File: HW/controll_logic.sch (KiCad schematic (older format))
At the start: 11 parts, among them SW1 RESET, U10 TL7705B, U9 74HC74, X2 8MHz

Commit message: Address, databus and control signals added to RAM and ROM
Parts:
- added U?: ispMACH4A, symbol ispMACH4A
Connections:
- net labels added: ~DUARTSEL, ~RTCSEL, ~VIA1SEL, ~VIA2SEL
- wire segments 60 -> 74
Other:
- moved on the sheet: SW1
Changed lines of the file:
@@
 encoding utf-8
 Sheet 5 6
-Title ""
-Date ""
-Rev ""
-Comp ""
+Title "Glue and control logic"
+Date "2017-12-23"
+Rev "0.1"
+Comp "Linux Grotto"
 Comment1 ""
 Comment2 ""
@@
 L R_Network07 RN2
 U 1 1 5A3B46CC
-P 6600 1550
-F 0 "RN2" V 6200 1550 50  0000 C CNN
-F 1 "3.3kOhm" V 7000 1550 50  0000 C CNN
-F 2 "Resistors_THT:R_Array_SIP8" V 7075 1550 50  0001 C CNN
-F 3 "" H 6600 1550 50  0001 C CNN
-	1    6600 1550
+P 1750 1100
+F 0 "RN2" V 1350 1100 50  0000 C CNN
+F 1 "3.3kOhm" V 2150 1100 50  0000 C CNN
+F 2 "Resistors_THT:R_Array_SIP8" V 2225 1100 50  0001 C CNN
+F 3 "" H 1750 1100 50  0001 C CNN
+	1    1750 1100
 	1    0    0    -1
 $EndComp
@@
 CLK
 NoConn ~ 2350 6625
-Wire Wire Line
-	2950 6625 3225 6625
-Wire Wire Line
-	2650 6075 2650 6325
-Wire Wire Line
-	2650 6075 3825 6075
-Wire Wire Line
-	3825 7175 3075 7175
-Wire Wire Line
-	3075 7175 3075 6075
-Connection ~ 3075 6075
-Wire Wire Line
-	4425 6825 4575 6825
-Wire Wire Line
-	4575 6825 4575 5975
-Wire Wire Line
-	4575 5975 3225 5975
-Wire Wire Line
-	3225 5975 3225 6425
-Wire Wire Line
-	4425 6425 4850 6425
-Wire Wire Line
-	2650 6925 2650 7050
-Wire Wire Line
-	1300 6075 700  6075
-Wire Wire Line
-	700  6075 700  7375
-Connection ~ 700  6425
-Connection ~ 700  6625
-Wire Wire Line
-	1300 7175 700  7175
-Connection ~ 700  7175
 NoConn ~ 1900 6425
 NoConn ~ 1900 6825
@@
 	1    0    0    -1
 $EndComp
-Wire Wire Line
-	3925 1350 3925 1150
-Wire Wire Line
-	4525 1750 4525 1925
-Wire Wire Line
-	4525 1925 4750 1925
-Wire Wire Line
-	4425 1750 4425 2025
-Wire Wire Line
-	4425 2025 4750 2025
-Wire Wire Line
-	4325 1750 4325 2125
-Wire Wire Line
-	4325 2125 4750 2125
-Wire Wire Line
-	4225 1750 4225 2225
-Wire Wire Line
-	4225 2225 4750 2225
-Wire Wire Line
-	4125 1750 4125 2325
-Wire Wire Line
-	4125 2325 4750 2325
-Wire Wire Line
-	4025 1750 4025 2425
-Wire Wire Line
-	4025 2425 4750 2425
-Wire Wire Line
-	3925 1750 3925 2825
-Wire Wire Line
-	3925 2525 4750 2525
 Text HLabel 4750 1925 2    60   BiDi ~ 0
 ~IRQ
@@
 Text HLabel 4750 2325 2    60   Output ~ 0
 ~SO
-Connection ~ 3925 2525
 Text HLabel 4750 2625 2    60   Output ~ 0
 RES
-Wire Wire Line
-	3925 3050 4250 3050
-Wire Wire Line
-	4250 2625 4250 3375
-Wire Wire Line
-	4250 2625 4750 2625
 $Comp
 L C_Small C15
@@
 F 3 "" H 2000 3575 50  0001 C CNN
 	1    2000 3375
-	0    1    1    0
-$EndComp
-Wire Wire Line
-	2325 3275 2325 3375
-Wire Wire Line
-	2325 3575 2325 3650
+	0    -1   -1   0
+$EndComp
 $Comp
 L GND #PWR16
@@
 	1    0    0    -1
 $EndComp
-Wire Wire Line
-	2000 3850 4250 3850
-Wire Wire Line
-	3125 3850 3125 3600
 $Comp
 L VCC #PWR13
@@
 	1    0    0    -1
 $EndComp
-Wire Wire Line
-	2000 2500 3125 2500
+$Comp
+L VCC #PWR18
+U 1 1 5A3BAB89
+P 1450 700
+F 0 "#PWR18" H 1450 550 50  0001 C CNN
+F 1 "VCC" H 1450 850 50  0000 C CNN
+F 2 "" H 1450 700 50  0001 C CNN
+F 3 "" H 1450 700 50  0001 C CNN
+	1    1450 700
+	1    0    0    -1
+$EndComp
+Text HLabel 2300 1475 2    60   Input ~ 0
+TCK
+Text HLabel 2300 1575 2    60   Input ~ 0
+TMS
+Text HLabel 2300 1675 2    60   Input ~ 0
+TDI
+Text HLabel 2300 1775 2    60   Output ~ 0
+TDO
+Text HLabel 2300 1875 2    60   Output ~ 0
+~KS
+$Comp
+L ispMACH4A U?
+U 1 1 5A3F3D11
+P 8275 2325
+F 0 "U?" H 8275 3775 60  0000 C CNN
+F 1 "ispMACH4A" V 8275 1950 60  0000 C CNN
+F 2 "" H 7950 2300 60  0001 C CNN
+F 3 "" H 7950 2300 60  0001 C CNN
+	1    8275 2325
+	1    0    0    -1
+$EndComp
+Text HLabel 7250 3075 0    60   Output ~ 0
+~DUARTSEL
+Wire Wire Line
+	2950 6625 3225 6625
+Wire Wire Line
+	2650 6075 2650 6325
+Wire Wire Line
+	2650 6075 3075 6075
+Wire Wire Line
+	3075 6075 3825 6075
+Wire Wire Line
+	3825 7175 3075 7175
+Wire Wire Line
+	3075 7175 3075 6075
+Connection ~ 3075 6075
+Wire Wire Line
+	4425 6825 4575 6825
+Wire Wire Line
+	4575 6825 4575 5975
+Wire Wire Line
+	4575 5975 3225 5975
+Wire Wire Line
+	3225 5975 3225 6425
+Wire Wire Line
+	4425 6425 4850 6425
+Wire Wire Line
+	2650 6925 2650 7050
+Wire Wire Line
+	1300 6075 700  6075
+Wire Wire Line
+	700  6075 700  6425
+Wire Wire Line
+	700  6425 700  6625
+Wire Wire Line
+	700  6625 700  7175
+Wire Wire Line
+	700  7175 700  7375
+Connection ~ 700  6425
+Connection ~ 700  6625
+Wire Wire Line
+	1300 7175 700  7175
+Connection ~ 700  7175
+Wire Wire Line
+	3925 1350 3925 1150
+Wire Wire Line
+	4525 1750 4525 1925
+Wire Wire Line
+	4525 1925 4750 1925
+Wire Wire Line
+	4425 1750 4425 2025
+Wire Wire Line
+	4425 2025 4750 2025
+Wire Wire Line
+	4325 1750 4325 2125
+Wire Wire Line
+	4325 2125 4750 2125
+Wire Wire Line
+	4225 1750 4225 2225
+Wire Wire Line
+	4225 2225 4750 2225
+Wire Wire Line
+	4125 1750 4125 2325
+Wire Wire Line
+	4125 2325 4750 2325
+Wire Wire Line
+	4025 1750 4025 2425
+Wire Wire Line
+	4025 2425 4750 2425
+Wire Wire Line
+	3925 1750 3925 2525
+Wire Wire Line
+	3925 2525 3925 2825
+Wire Wire Line
+	3925 2525 4750 2525
+Connection ~ 3925 2525
+Wire Wire Line
+	3925 3050 4250 3050
+Wire Wire Line
+	4250 2625 4250 3050
+Wire Wire Line
+	4250 3050 4250 3375
+Wire Wire Line
+	4250 2625 4750 2625
+Wire Wire Line
+	2325 3275 2325 3375
+Wire Wire Line
+	2325 3575 2325 3650
+Wire Wire Line
+	2000 3850 2325 3850
+Wire Wire Line
+	2325 3850 3125 3850
+Wire Wire Line
+	3125 3850 3925 3850
+Wire Wire Line
+	3925 3850 4250 3850
+Wire Wire Line
+	3125 3850 3125 3600
+Wire Wire Line
+	2000 2500 2325 2500
+Wire Wire Line
+	2325 2500 3125 2500
 Wire Wire Line
 	2325 2500 2325 2825
@@
 	4250 3850 4250 3575
 Connection ~ 3925 3850
-$Comp
-L VCC #PWR18
-U 1 1 5A3BAB89
-P 6300 1150
-F 0 "#PWR18" H 6300 1000 50  0001 C CNN
-F 1 "VCC" H 6300 1300 50  0000 C CNN
-F 2 "" H 6300 1150 50  0001 C CNN
-F 3 "" H 6300 1150 50  0001 C CNN
-	1    6300 1150
-	1    0    0    -1
-$EndComp
-Wire Wire Line
-	6300 1350 6300 1150
-Wire Wire Line
-	6900 1750 6900 1925
-Wire Wire Line
-	6900 1925 7150 1925
-Wire Wire Line
-	6800 1750 6800 2025
-Wire Wire Line
-	6800 2025 7150 2025
-Wire Wire Line
-	6700 1750 6700 2125
-Wire Wire Line
-	6700 2125 7150 2125
-Wire Wire Line
-	6600 1750 6600 2225
-Wire Wire Line
-	6600 2225 7150 2225
-Wire Wire Line
-	6500 1750 6500 2325
-Wire Wire Line
-	6500 2325 7150 2325
-Wire Wire Line
-	6400 1750 6400 2425
-Wire Wire Line
-	6400 2425 7150 2425
-Wire Wire Line
-	6300 1750 6300 2525
-Wire Wire Line
-	6300 2525 7150 2525
-Text HLabel 7150 1925 2    60   Input ~ 0
-TCK
-Text HLabel 7150 2025 2    60   Input ~ 0
-TMS
-Text HLabel 7150 2125 2    60   Input ~ 0
-TDI
-Text HLabel 7150 2225 2    60   Output ~ 0
-TDO
-Text HLabel 7150 2325 2    60   Output ~ 0
-~KS
+Wire Wire Line
+	1450 900  1450 700
+Wire Wire Line
+	2050 1300 2050 1475
+Wire Wire Line
+	2050 1475 2300 1475
+Wire Wire Line
+	1950 1300 1950 1575
+Wire Wire Line
+	1950 1575 2300 1575
+Wire Wire Line
+	1850 1300 1850 1675
+Wire Wire Line
+	1850 1675 2300 1675
+Wire Wire Line
+	1750 1300 1750 1775
+Wire Wire Line
+	1750 1775 2300 1775
+Wire Wire Line
+	1650 1300 1650 1875
+Wire Wire Line
+	1650 1875 2300 1875
+Wire Wire Line
+	1550 1300 1550 1975
+Wire Wire Line
+	1550 1975 2300 1975
+Wire Wire Line
+	1450 1300 1450 2075
+Wire Wire Line
+	1450 2075 2300 2075
+Wire Wire Line
+	7550 3075 7250 3075
+Wire Wire Line
+	7550 3200 7250 3200
+Wire Wire Line
+	7550 3325 7250 3325
+Wire Wire Line
+	7550 3450 7250 3450
+Text HLabel 7250 3200 0    60   Output ~ 0
+~VIA1SEL
+Text HLabel 7250 3325 0    60   Output ~ 0
+~VIA2SEL
+Text HLabel 7250 3450 0    60   Output ~ 0
+~RTCSEL
 $EndSCHEMATC

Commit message: Small changes.
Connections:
- net labels added: ~ABT
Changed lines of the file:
@@
 Text HLabel 7250 3450 0    60   Output ~ 0
 ~RTCSEL
+Text HLabel 2300 1975 2    60   Output ~ 0
+~ABT
 $EndSCHEMATC

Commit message: Added address decoding.
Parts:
- removed RN1, RN2: 3.3kOhm, Resistors_THT:R_Array_SIP8, symbol R_Network07
- added RN?: 3.3k, Resistors_THT:R_Array_SIP9, symbol R_Network08
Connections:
- net labels removed: ~SO
- wire segments 74 -> 51
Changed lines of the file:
@@
-$EndComp
-$Comp
-L R_Network07 RN1
-U 1 1 5A3B464D
-P 4225 1550
-F 0 "RN1" V 3825 1550 50  0000 C CNN
-F 1 "3.3kOhm" V 4625 1550 50  0000 C CNN
-F 2 "Resistors_THT:R_Array_SIP8" V 4700 1550 50  0001 C CNN
-F 3 "" H 4225 1550 50  0001 C CNN
-	1    4225 1550
-	1    0    0    -1
-$EndComp
-$Comp
-L R_Network07 RN2
-U 1 1 5A3B46CC
-P 1750 1100
-F 0 "RN2" V 1350 1100 50  0000 C CNN
-F 1 "3.3kOhm" V 2150 1100 50  0000 C CNN
-F 2 "Resistors_THT:R_Array_SIP8" V 2225 1100 50  0001 C CNN
-F 3 "" H 1750 1100 50  0001 C CNN
-	1    1750 1100
-	1    0    0    -1
 $EndComp
 $Comp
@@
 Text HLabel 4750 2525 2    60   Output ~ 0
 ~RES
-Text HLabel 4750 2325 2    60   Output ~ 0
-~SO
 Text HLabel 4750 2625 2    60   Output ~ 0
 RES
@@
 	1    0    0    -1
 $EndComp
-$Comp
-L VCC #PWR18
-U 1 1 5A3BAB89
-P 1450 700
-F 0 "#PWR18" H 1450 550 50  0001 C CNN
-F 1 "VCC" H 1450 850 50  0000 C CNN
-F 2 "" H 1450 700 50  0001 C CNN
-F 3 "" H 1450 700 50  0001 C CNN
-	1    1450 700
-	1    0    0    -1
-$EndComp
-Text HLabel 2300 1475 2    60   Input ~ 0
+Text HLabel 9950 3675 2    60   Input ~ 0
 TCK
-Text HLabel 2300 1575 2    60   Input ~ 0
+Text HLabel 9950 3775 2    60   Input ~ 0
 TMS
-Text HLabel 2300 1675 2    60   Input ~ 0
+Text HLabel 9950 3875 2    60   Input ~ 0
 TDI
-Text HLabel 2300 1775 2    60   Output ~ 0
+Text HLabel 9950 3975 2    60   Output ~ 0
 TDO
-Text HLabel 2300 1875 2    60   Output ~ 0
+Text HLabel 4750 1825 2    60   Output ~ 0
 ~KS
 $Comp
@@
 	2650 6075 2650 6325
 Wire Wire Line
-	2650 6075 3075 6075
-Wire Wire Line
-	3075 6075 3825 6075
+	2650 6075 3825 6075
 Wire Wire Line
 	3825 7175 3075 7175
@@
 	1300 6075 700  6075
 Wire Wire Line
-	700  6075 700  6425
-Wire Wire Line
-	700  6425 700  6625
-Wire Wire Line
-	700  6625 700  7175
-Wire Wire Line
-	700  7175 700  7375
+	700  6075 700  7375
 Connection ~ 700  6425
 Connection ~ 700  6625
@@
 	4025 2425 4750 2425
 Wire Wire Line
-	3925 1750 3925 2525
-Wire Wire Line
-	3925 2525 3925 2825
+	3925 1750 3925 2825
 Wire Wire Line
 	3925 2525 4750 2525
@@
 	3925 3050 4250 3050
 Wire Wire Line
-	4250 2625 4250 3050
-Wire Wire Line
-	4250 3050 4250 3375
+	4250 2625 4250 3375
 Wire Wire Line
 	4250 2625 4750 2625
@@
 	2325 3575 2325 3650
 Wire Wire Line
-	2000 3850 2325 3850
-Wire Wire Line
-	2325 3850 3125 3850
-Wire Wire Line
-	3125 3850 3925 3850
-Wire Wire Line
-	3925 3850 4250 3850
+	2000 3850 4250 3850
 Wire Wire Line
 	3125 3850 3125 3600
 Wire Wire Line
-	2000 2500 2325 2500
-Wire Wire Line
-	2325 2500 3125 2500
+	2000 2500 3125 2500
 Wire Wire Line
 	2325 2500 2325 2825
@@
 	4250 3850 4250 3575
 Connection ~ 3925 3850
-Wire Wire Line
-	1450 900  1450 700
-Wire Wire Line
-	2050 1300 2050 1475
-Wire Wire Line
-	2050 1475 2300 1475
-Wire Wire Line
-	1950 1300 1950 1575
-Wire Wire Line
-	1950 1575 2300 1575
-Wire Wire Line
-	1850 1300 1850 1675
-Wire Wire Line
-	1850 1675 2300 1675
-Wire Wire Line
-	1750 1300 1750 1775
-Wire Wire Line
-	1750 1775 2300 1775
-Wire Wire Line
-	1650 1300 1650 1875
-Wire Wire Line
-	1650 1875 2300 1875
-Wire Wire Line
-	1550 1300 1550 1975
-Wire Wire Line
-	1550 1975 2300 1975
-Wire Wire Line
-	1450 1300 1450 2075
-Wire Wire Line
-	1450 2075 2300 2075
 Wire Wire Line
 	7550 3075 7250 3075
@@
 Text HLabel 7250 3450 0    60   Output ~ 0
 ~RTCSEL
-Text HLabel 2300 1975 2    60   Output ~ 0
+Text HLabel 4750 2325 2    60   Output ~ 0
 ~ABT
+$Comp
+L R_Network08 RN?
+U 1 1 5A416FA2
+P 4325 1550
+F 0 "RN?" V 3825 1550 50  0000 C CNN
+F 1 "3.3k" H 4275 1725 50  0000 C CNN
+F 2 "Resistors_THT:R_Array_SIP9" V 4800 1550 50  0001 C CNN
+F 3 "" H 4325 1550 50  0001 C CNN
+	1    4325 1550
+	1    0    0    -1
+$EndComp
+Wire Wire Line
+	4625 1750 4625 1825
+Wire Wire Line
+	4625 1825 4750 1825
 $EndSCHEMATC

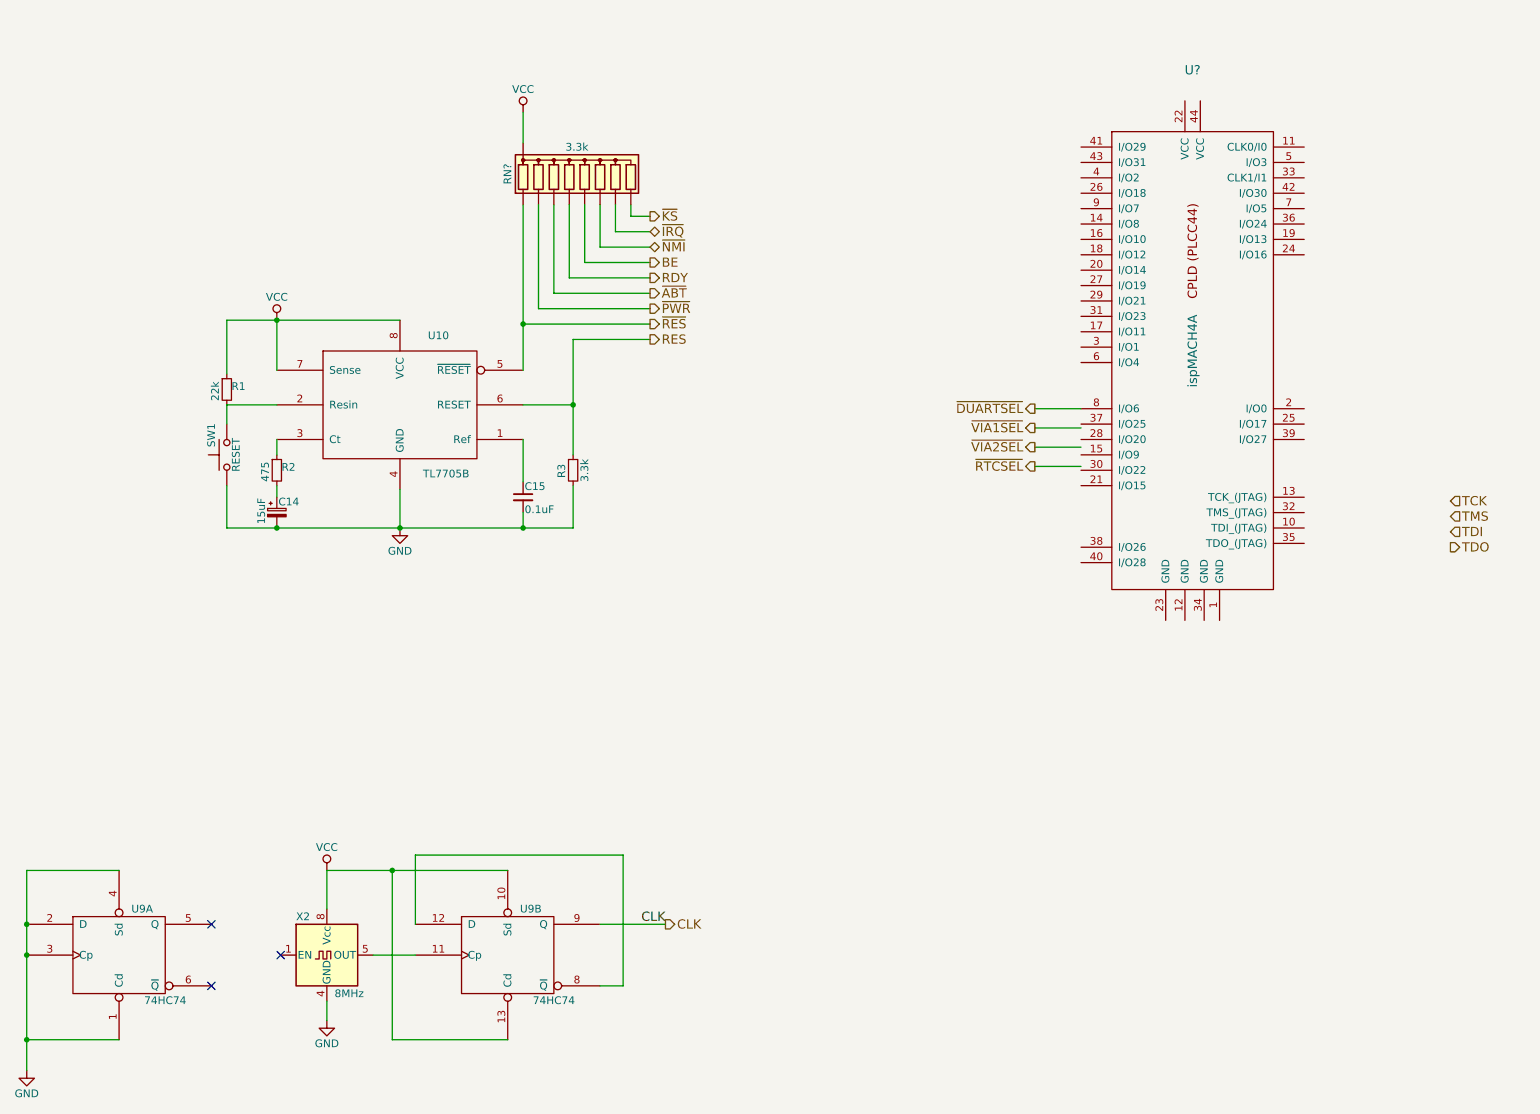
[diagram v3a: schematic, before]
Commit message: Simulation of address decoding.
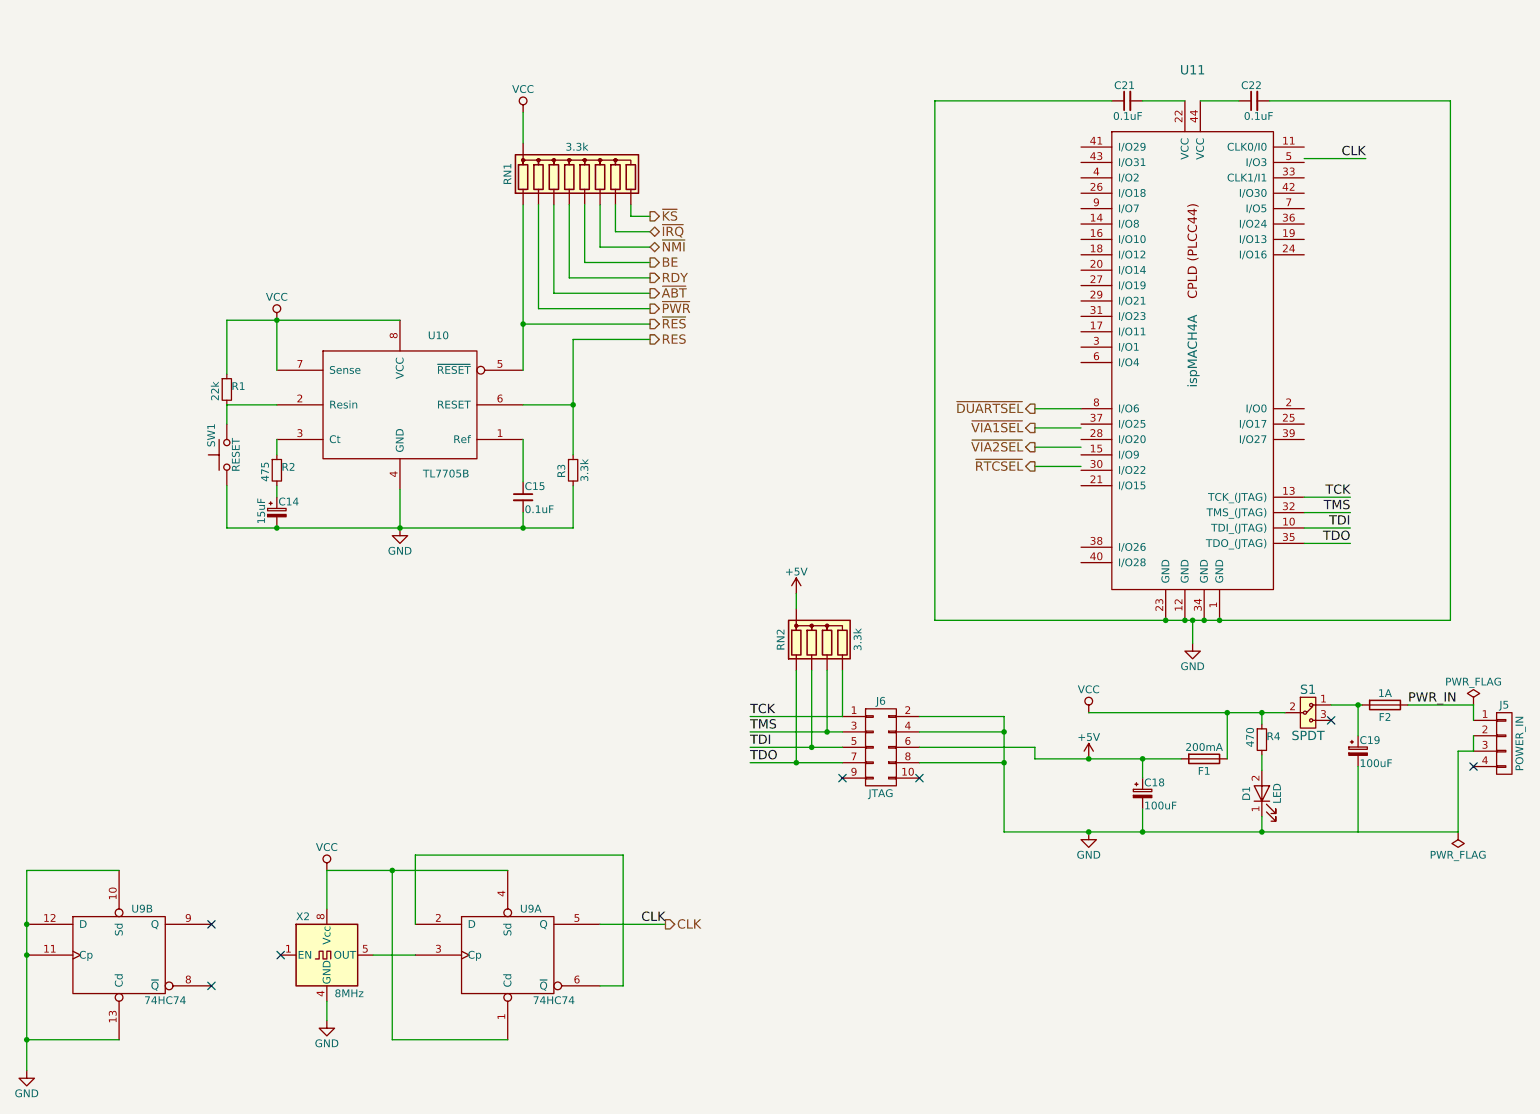
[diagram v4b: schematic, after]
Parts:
- added C18, C19: 100uF, symbol CP_Small
- added C21, C22: 0.1uF, symbol C_Small
- added D1: LED, symbol LED
- added F1: 200mA, symbol Fuse
- added F2: 1A, symbol Fuse
- added J5: POWER_IN, symbol CONN_01X04
- added J6: JTAG, symbol CONN_02X05
- added R4: 470, symbol R_Small
- added RN2: 3.3k, Resistors_THT:R_Array_SIP5, symbol R_Network04
- added S1: SPDT, symbol SPDT
- gave numbers to parts that had none: 2
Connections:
- net labels added: +5V, PWR_IN
- wire segments 51 -> 96
- no-connect marks 3 -> 7
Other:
- moved on the sheet: U9A, U9B

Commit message: ABEL code passes compilation, no tests though. Small changes to schema
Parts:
- added J8: Stop System, Pin_Headers:Pin_Header_Straight_1x03_Pitch2.54mm, symbol CONN_01X03
- C14: footprint (none) -> Capacitors_ThroughHole:CP_Radial_D5.0mm_P2.50mm
- C15, C21, C22: footprint (none) -> Capacitors_ThroughHole:C_Disc_D4.7mm_W2.5mm_P5.00mm
- C18, C19: footprint (none) -> Capacitors_ThroughHole:CP_Radial_D6.3mm_P2.50mm
- D1: footprint (none) -> LEDs:LED_D3.0mm
- F1, F2: footprint (none) -> Fuse_Holders_and_Fuses:Fuseholder5x20_horiz_open_Schurter_0031_8201
- J5: footprint (none) -> Connectors_Molex:Molex_NanoFit_1x04x2.50mm_Angled
- J6: footprint (none) -> Connectors_IDC:IDC-Header_2x05_Pitch2.54mm_Straight
- R1, R2, R3, R4: footprint (none) -> Resistors_ThroughHole:R_Axial_DIN0207_L6.3mm_D2.5mm_P2.54mm_Vertical
- S1: footprint (none) -> Switches_THT:SW-SPDT-0900766b81587629
- SW1: footprint (none) -> Buttons_Switches_ThroughHole:SW_PUSH_6mm_h4.3mm
- U10: footprint (none) -> Housings_DIP:DIP-8_W7.62mm_Socket
- U11: footprint (none) -> saturn:PLCC-44_THT-Socket
- U9: footprint (none) -> Housings_DIP:DIP-14_W7.62mm_Socket
- X2: value 8MHz -> 16MHz
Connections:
- net labels added: A10, A11, A12, A13, A14, A15, A16, A17, A18, A8, A9, A[0..18], D0, D1, D2, D3, D[0..7], R/~W, RAM0, RAM1, ROM, STP, VDA, VPA, ~MRD, ~MWR, ~RAM0, ~RAM1, ~ROM, ~UARTSEL
- wire segments 96 -> 154
- no-connect marks 7 -> 10
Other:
- note added: "Clock generator"
- note added: "RESET controller"
